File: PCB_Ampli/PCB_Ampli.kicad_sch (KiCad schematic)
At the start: 0 parts

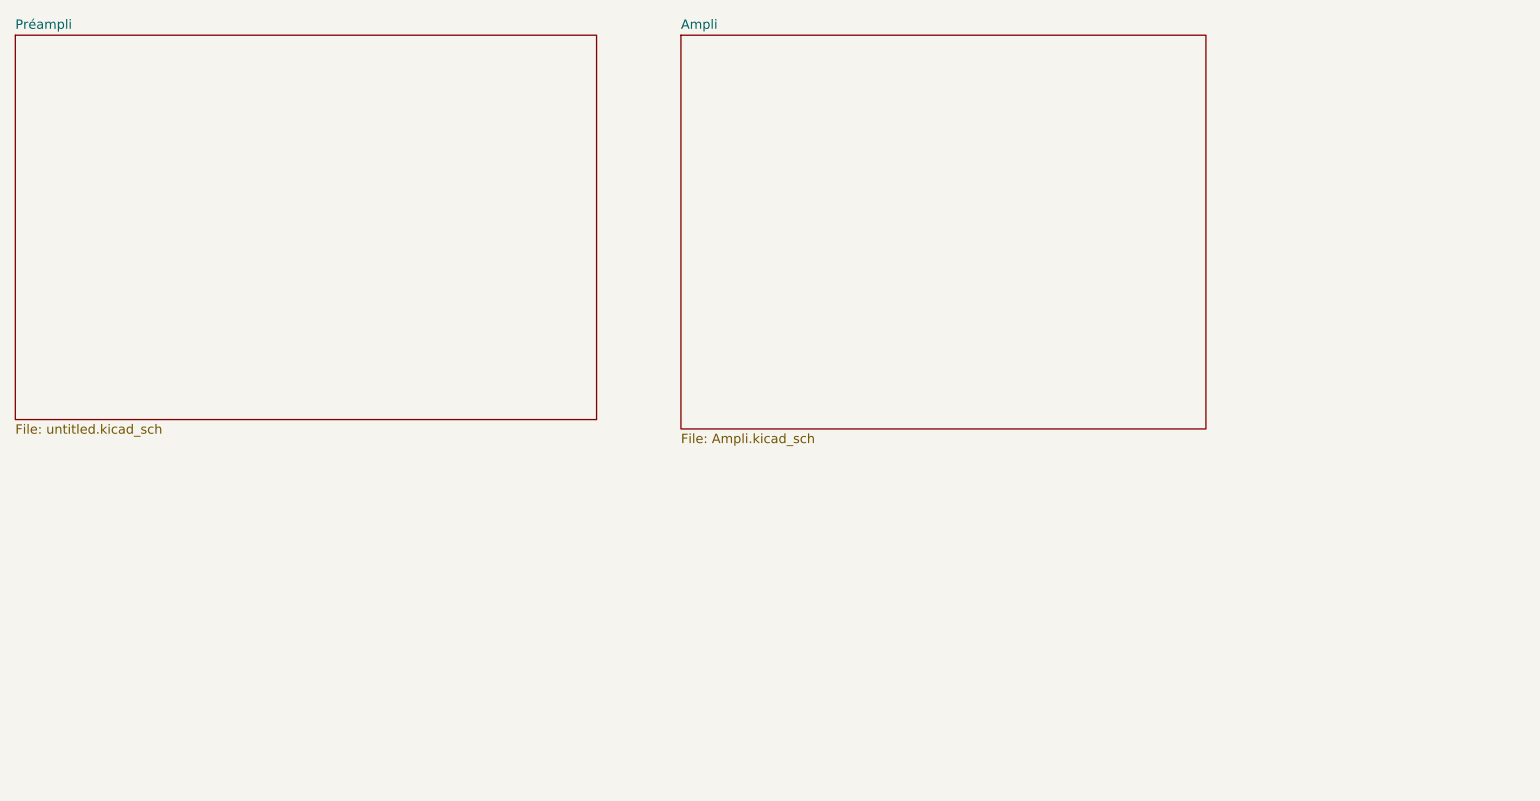
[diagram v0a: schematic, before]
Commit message: PCBV2_Part_Ampli_done
Amplification part using TPA3255 done
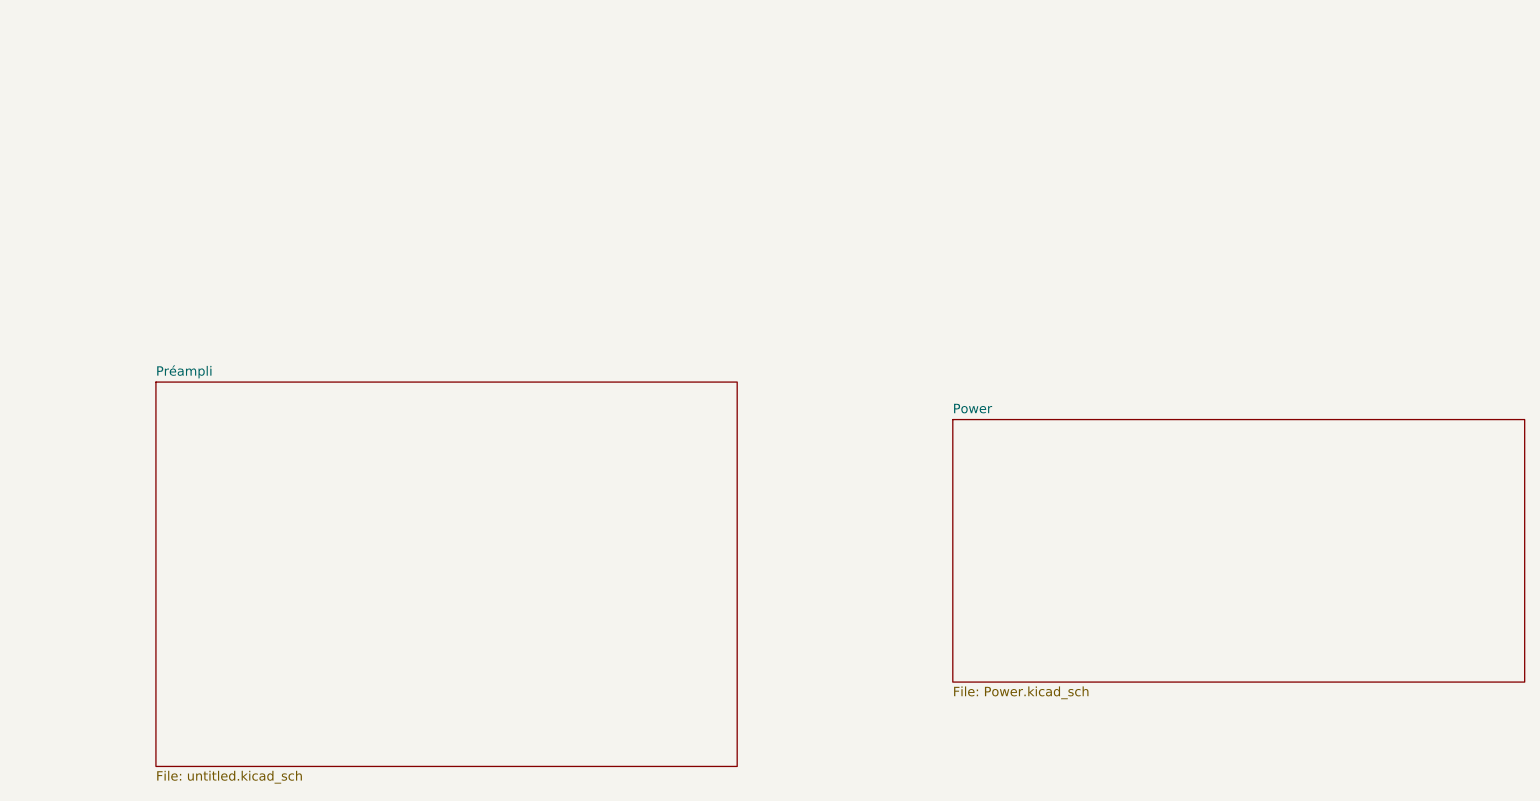
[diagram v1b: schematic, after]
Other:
- removed sheet Ampli
- added sheet Power (Power.kicad_sch)
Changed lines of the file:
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@@
     (comment 1 "CAILLAUD Paul")
   )
-  (sheet (at 25.4 21.59) (size 78.74 52.07) (fields_autoplaced)
+  (sheet (at 152.4 73.66) (size 77.47 35.56) (fields_autoplaced)
     (stroke (width 0.1524) (type solid))
     (fill (color 0 0 0 0.0000))
-    (property "Sheetname" "Préampli" (at 25.4 20.8784 0)
+    (property "Sheetname" "Power" (at 152.4 72.9484 0)
       (effects (font (size 1.27 1.27)) (justify left bottom))
     )
-    (property "Sheetfile" "untitled.kicad_sch" (at 25.4 74.2446 0)
+    (property "Sheetfile" "Power.kicad_sch" (at 152.4 109.8046 0)
+      (effects (font (size 1.27 1.27)) (justify left top))
+    )
+    (instances
+      (project "PCB_Ampli"
+        (path "/3526ba72-9b59-4427-a8d2-8259ce6cbf48" (page "4"))
+      )
+    )
+  )
+  (sheet (at 44.45 68.58) (size 78.74 52.07) (fields_autoplaced)
+    (stroke (width 0.1524) (type solid))
+    (fill (color 0 0 0 0.0000))
+    (property "Sheetname" "Préampli" (at 44.45 67.8684 0)
+      (effects (font (size 1.27 1.27)) (justify left bottom))
+    )
+    (property "Sheetfile" "untitled.kicad_sch" (at 44.45 121.2346 0)
       (effects (font (size 1.27 1.27)) (justify left top))
     )
@@
       )
     )
-  )
-  (sheet (at 115.57 21.59) (size 71.12 53.34) (fields_autoplaced)
-    (stroke (width 0.1524) (type solid))
-    (fill (color 0 0 0 0.0000))
-    (property "Sheetname" "Ampli" (at 115.57 20.8784 0)
-      (effects (font (size 1.27 1.27)) (justify left bottom))
-    )
-    (property "Sheetfile" "Ampli.kicad_sch" (at 115.57 75.5146 0)
-      (effects (font (size 1.27 1.27)) (justify left top))
-    )
-    (instances
-      (project "PCB_Ampli"
-        (path "/3526ba72-9b59-4427-a8d2-8259ce6cbf48" (page "3"))
-      )
-    )
